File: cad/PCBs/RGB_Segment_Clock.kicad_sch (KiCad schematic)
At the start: 10 parts, among them J1 TYPE-C-31-M-12, U1 BH1750FVI-TR, U2 HDC2080, U3 74HC595, U4 74HC595

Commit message: Initial Digit Schematic and Layout
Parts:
- removed A1: RaspberryPi_Pico_W, Module_RaspberryPi_Pico:RaspberryPi_Pico_Common, symbol MCU_Module_RaspberryPi_Pico:RaspberryPi_Pico_W
- removed D1: SK6812, LED_SMD:LED_SK6812_PLCC4_5.0x5.0mm_P3.2mm, symbol LED:SK6812
- removed J1: TYPE-C-31-M-12, TYPE-C-31-M-12:HRO_TYPE-C-31-M-12, symbol TYPE-C-31-M-12:TYPE-C-31-M-12
- removed R1, R2: 5.1k, Resistor_SMD:R_2010_5025Metric, symbol Device:R
- removed SZ720788W1: ~, symbol SZ720788W-64:SZ720788W-64
- removed U1: BH1750FVI-TR, BH1750FVI-TR:XDCR_BH1750FVI-TR, symbol BH1750FVI-TR:BH1750FVI-TR
- removed U2: HDC2080, Package_SON:Texas_PWSON-N6, symbol Sensor_Humidity:HDC2080
- removed U3, U4: 74HC595, symbol 74xx:74HC595
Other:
- added sheet Controller (Controller/Controller.kicad_sch)
- added sheet Tick (Tick/Tick.kicad_sch)
- sheet Digit ports: added BL_IN, BL_OUT, DIGIT_IN, DIGIT_OUT, GND_IN, GND_OUT, VCC_IN, VCC_OUT; removed none
- title: (none) -> RGB Clock Assembly

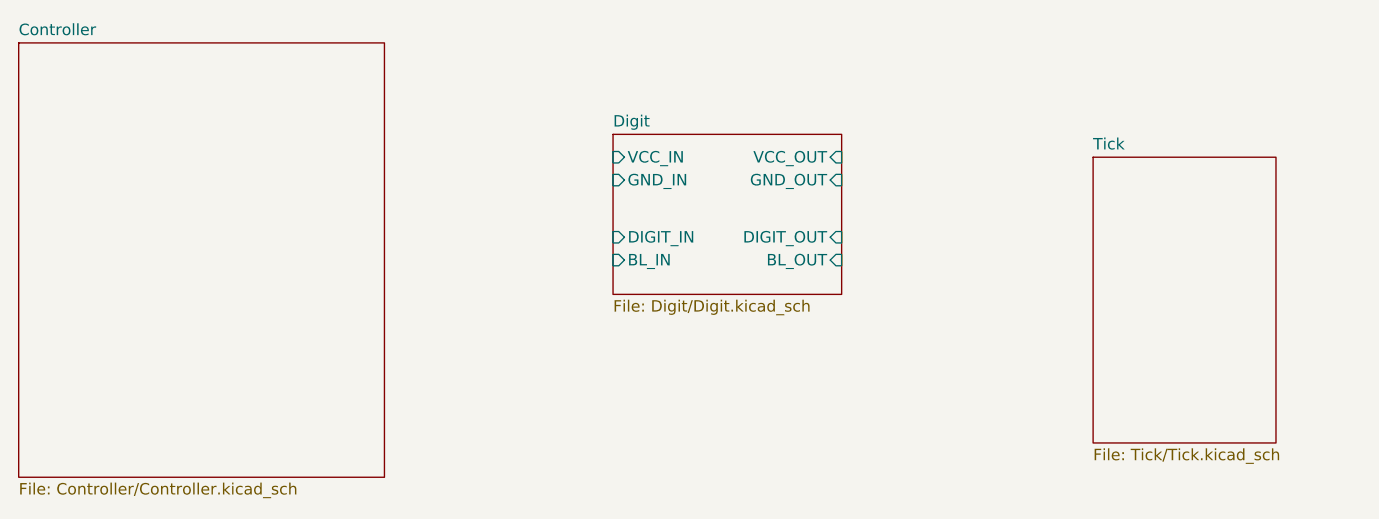
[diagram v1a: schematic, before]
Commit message: Connected Controller Components, updated matrix footprint
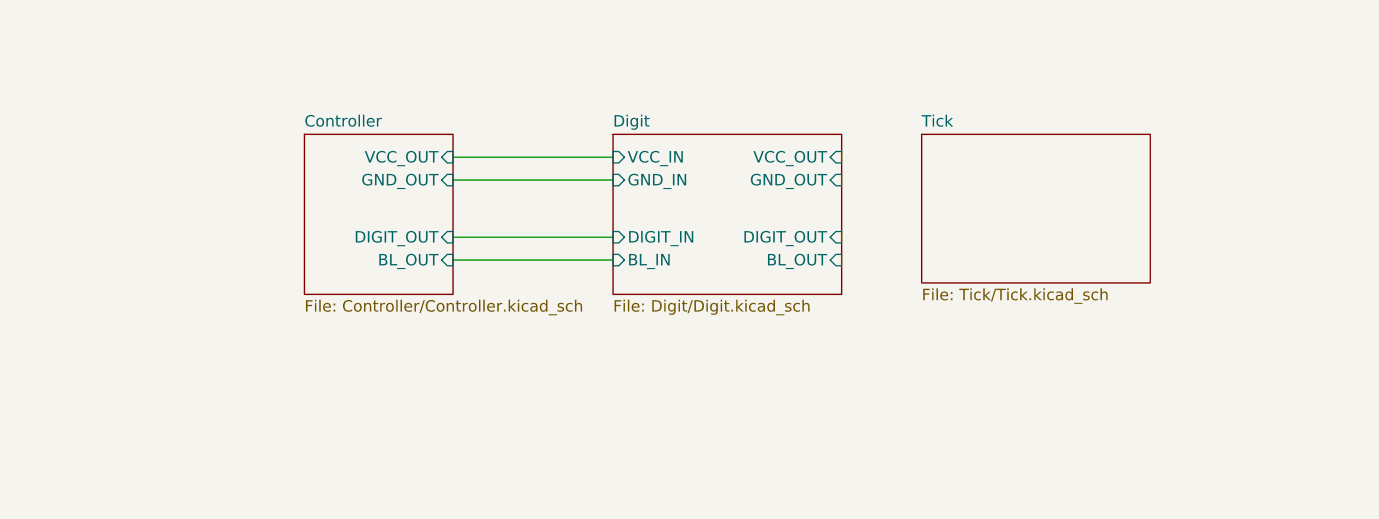
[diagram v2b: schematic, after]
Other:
- sheet Controller ports: added BL_OUT, DIGIT_OUT, GND_OUT, VCC_OUT; removed none
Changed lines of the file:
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@@
 		(title "RGB Clock Assembly")
 	)
+	(wire
+		(pts
+			(xy 82.55 80.01) (xy 100.33 80.01)
+		)
+		(stroke
+			(width 0)
+			(type default)
+		)
+	)
+	(wire
+		(pts
+			(xy 82.55 88.9) (xy 100.33 88.9)
+		)
+		(stroke
+			(width 0)
+			(type default)
+		)
+	)
+	(wire
+		(pts
+			(xy 82.55 86.36) (xy 100.33 86.36)
+		)
+		(stroke
+			(width 0)
+			(type default)
+		)
+	)
+	(wire
+		(pts
+			(xy 82.55 77.47) (xy 100.33 77.47)
+		)
+		(stroke
+			(width 0)
+			(type default)
+		)
+	)
 	(sheet
-		(at 34.29 64.77)
-		(size 40.64 48.26)
+		(at 66.04 74.93)
+		(size 16.51 17.78)
 		(fields_autoplaced yes)
 		(stroke
@@
 		)
 		(property "Sheetname" "Controller"
-			(at 34.29 64.0584 0)
+			(at 66.04 74.2184 0)
 			(effects
 				(font
@@
 		)
 		(property "Sheetfile" "Controller/Controller.kicad_sch"
-			(at 34.29 113.6146 0)
+			(at 66.04 93.2946 0)
 			(effects
 				(font
@@
 				)
 				(justify left top)
+			)
+		)
+		(pin "DIGIT_OUT" input
+			(at 82.55 86.36 0)
+			(effects
+				(font
+					(size 1.27 1.27)
+				)
+				(justify right)
+			)
+		)
+		(pin "BL_OUT" input
+			(at 82.55 88.9 0)
+			(effects
+				(font
+					(size 1.27 1.27)
+				)
+				(justify right)
+			)
+		)
+		(pin "VCC_OUT" input
+			(at 82.55 77.47 0)
+			(effects
+				(font
+					(size 1.27 1.27)
+				)
+				(justify right)
+			)
+		)
+		(pin "GND_OUT" input
+			(at 82.55 80.01 0)
+			(effects
+				(font
+					(size 1.27 1.27)
+				)
+				(justify right)
 			)
 		)
@@
 	)
 	(sheet
-		(at 153.67 77.47)
-		(size 20.32 31.75)
+		(at 134.62 74.93)
+		(size 25.4 16.51)
 		(fields_autoplaced yes)
 		(stroke
@@
 		)
 		(property "Sheetname" "Tick"
-			(at 153.67 76.7584 0)
+			(at 134.62 74.2184 0)
 			(effects
 				(font
@@
 		)
 		(property "Sheetfile" "Tick/Tick.kicad_sch"
-			(at 153.67 109.8046 0)
+			(at 134.62 92.0246 0)
 			(effects
 				(font
